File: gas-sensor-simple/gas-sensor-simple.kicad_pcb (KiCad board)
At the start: 2 copper layers, 29 parts, among them J1 8-pin male, U1 MQ-8, U10 MV5x3x, U11 MV5x3x, U12 LM393, U13 ads1x15, U14 ads1x15, U15 BME280, U2 MQ-4, U3 CO2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

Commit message: Minor change to pcb
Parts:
- moved R8 3.81 mm to (171.4, 138.4)
- moved R2 2.54 mm to (171.4, 96.5)
- moved R4 2.54 mm to (171.4, 110.5)
- moved R6 2.54 mm to (171.4, 124.5)
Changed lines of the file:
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@@
     (links 89)
     (no_connects 89)
-    (area 94.431429 79.964999 179.491905 150.725)
+    (area 102.051429 78.694999 183.301905 150.725)
     (thickness 1.6)
     (drawings 0)
@@
     (pad_to_mask_clearance 0.2)
     (aux_axis_origin 0 0)
-    (visible_elements FFFFF77F)
+    (visible_elements 7FFFFFFF)
     (pcbplotparams
       (layerselection 0x00030_80000001)
@@
   )
   (module Resistors_THT:R_Axial_DIN0207_L6.3mm_D2.5mm_P10.16mm_Horizontal (layer F.Cu)
-    (at 171.45 93.98 90)
+    (at 171.45 96.52 90)
     (descr "Resistor, Axial_DIN0207 series, Axial, Horizontal, pin pitch=10.16mm, 0.25W = 1/4W, length*diameter=6.3*2.5mm^2, http://cdn-reichelt.de/documents/datenblatt/B400/1_4W%23YAG.pdf")
     (tags "Resistor Axial_DIN0207 series Axial Horizontal pin pitch 10.16mm 0.25W = 1/4W length 6.3mm diameter 2.5mm")
@@
   )
   (module Resistors_THT:R_Axial_DIN0207_L6.3mm_D2.5mm_P10.16mm_Horizontal (layer F.Cu)
-    (at 171.45 107.95 90)
+    (at 171.45 110.49 90)
     (descr "Resistor, Axial_DIN0207 series, Axial, Horizontal, pin pitch=10.16mm, 0.25W = 1/4W, length*diameter=6.3*2.5mm^2, http://cdn-reichelt.de/documents/datenblatt/B400/1_4W%23YAG.pdf")
     (tags "Resistor Axial_DIN0207 series Axial Horizontal pin pitch 10.16mm 0.25W = 1/4W length 6.3mm diameter 2.5mm")
@@
   )
   (module Resistors_THT:R_Axial_DIN0207_L6.3mm_D2.5mm_P10.16mm_Horizontal (layer F.Cu)
-    (at 171.45 121.92 90)
+    (at 171.45 124.46 90)
     (descr "Resistor, Axial_DIN0207 series, Axial, Horizontal, pin pitch=10.16mm, 0.25W = 1/4W, length*diameter=6.3*2.5mm^2, http://cdn-reichelt.de/documents/datenblatt/B400/1_4W%23YAG.pdf")
     (tags "Resistor Axial_DIN0207 series Axial Horizontal pin pitch 10.16mm 0.25W = 1/4W length 6.3mm diameter 2.5mm")
@@
   )
   (module Resistors_THT:R_Axial_DIN0207_L6.3mm_D2.5mm_P10.16mm_Horizontal (layer F.Cu)
-    (at 171.45 134.62 90)
-    (descr "Resistor, Axial_DIN0207 series, Axial, Horizontal, pin pitch=10.16mm, 0.25W = 1/4W, length*diameter=6.3*2.5mm^2, http://cdn-reichelt.de/documents/datenblatt/B400/1_4W%23YAG.pdf")
-    (tags "Resistor Axial_DIN0207 series Axial Horizontal pin pitch 10.16mm 0.25W = 1/4W length 6.3mm diameter 2.5mm")
+    (at 171.45 138.43 90)
+    (descr "Resistor, Axial_DIN0207 series, Axial, Horizontal, pin pitch=10.16mm, 0.25W = 1/4W, length*diameter=6.3*2.5mm^2, http://cdn-reichelt.de/documents/datenblatt/B400/1_4W%23YAG.pdf")
+    (tags "Resistor Axial_DIN0207 series Axial Horizontal pin pitch 10.16mm 0.25W = 1/4W length 6.3mm diameter 2.5mm")

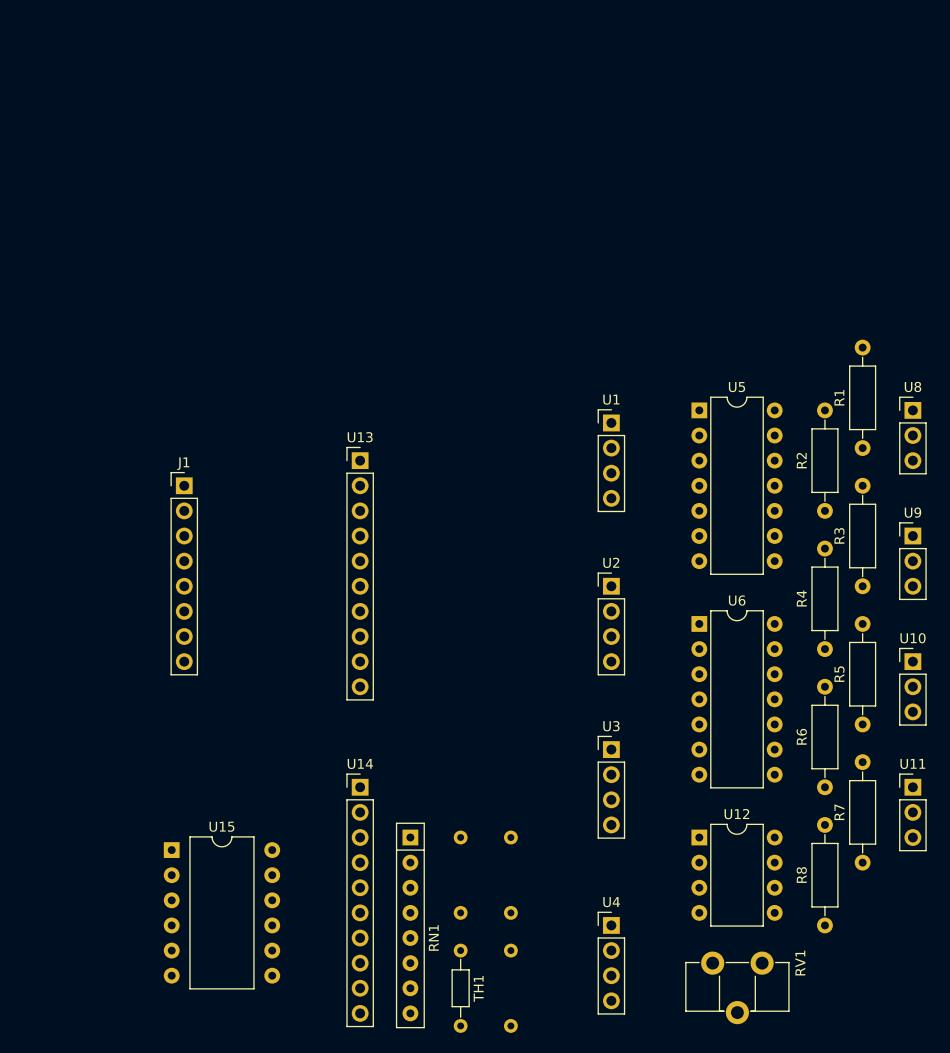
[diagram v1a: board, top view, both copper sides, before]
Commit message: Add back headers to separate analog board from digital.
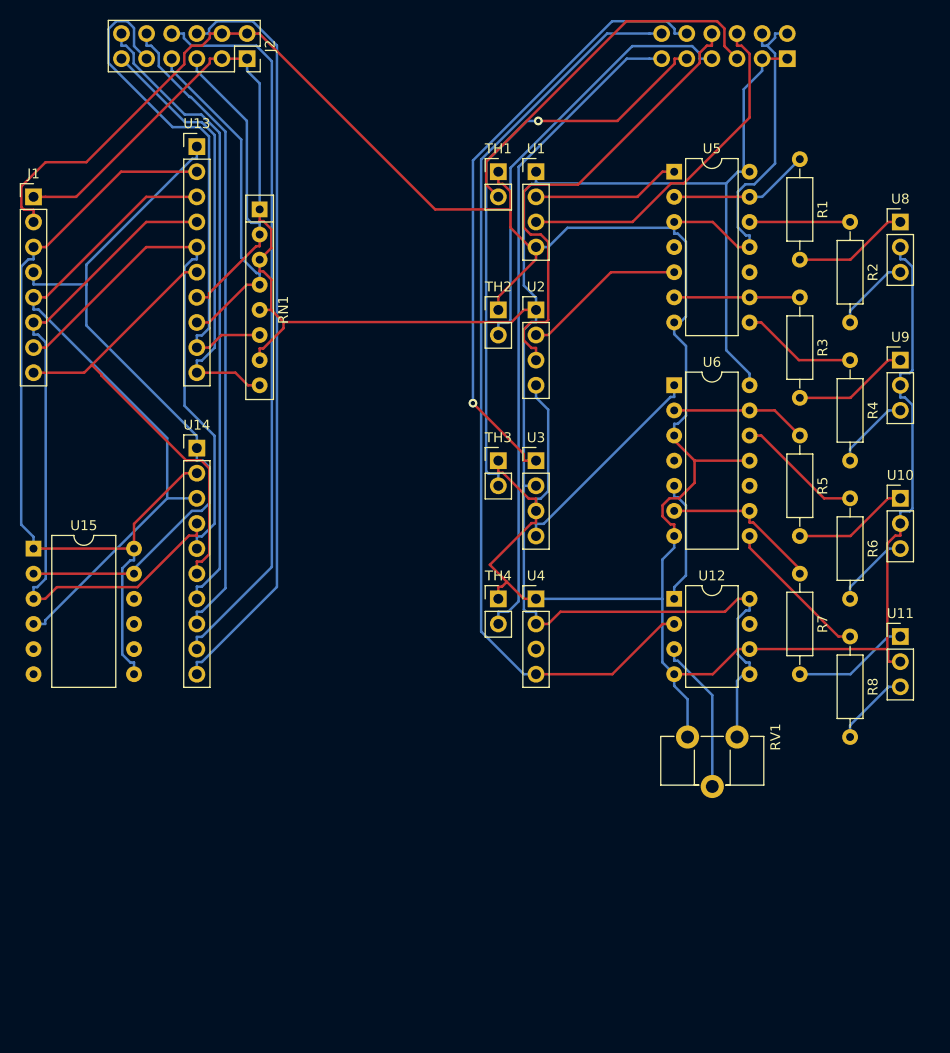
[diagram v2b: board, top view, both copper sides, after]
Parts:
- added J2: 2 x 6 pin female, Socket_Strips:Socket_Strip_Straight_2x06_Pitch2.54mm, F.Cu at (113.0, 50.8)
- added J3: 2 x 6 pin male, Pin_Headers:Pin_Header_Straight_2x06_Pitch2.54mm, B.Cu at (167.6, 50.8)
- J1: value 8-pin male -> 8-pin
- TH1: footprint Resistors_THT:R_Axial_DIN0204_L3.6mm_D1.6mm_P7.62mm_Horizontal -> Socket_Strips:Socket_Strip_Straight_1x02_Pitch2.54mm
- TH2, TH3, TH4: footprint Resistors_THT:R_Axial_DIN0204_L3.6mm_D1.6mm_P7.62mm_Horizontal -> Socket_Strips:Socket_Strip_Straight_1x02_Pitch2.54mm; moved to F.Cu
- U3: value CO2 -> DFRobotCO2; footprint Pin_Headers:Pin_Header_Straight_1x04_Pitch2.54mm -> Socket_Strips:Socket_Strip_Straight_1x04_Pitch2.54mm
- moved TH1 78.8 mm to (138.4, 62.2), turned to 0 degrees
- moved RN1 65.3 mm to (114.3, 66.0)
- moved TH2 53.4 mm to (138.4, 76.2), turned to 0 degrees
- moved TH3 38.3 mm to (138.4, 91.4), turned to 0 degrees
- moved U14 38.1 mm to (108.0, 90.2)
- moved U13 35.8 mm to (108.0, 59.7)
- moved TH4 35.6 mm to (138.4, 105.4), turned to 0 degrees
- moved U4 33.9 mm to (142.2, 105.4)
- moved U15 33.5 mm to (91.4, 100.3)
- moved J1 32.9 mm to (91.4, 64.8)
- moved U3 30.2 mm to (142.2, 91.4)
- moved R7 29.9 mm to (168.9, 102.9), turned to 270 degrees
- moved R1 29.9 mm to (168.9, 61.0), turned to 270 degrees
- moved R3 29.9 mm to (168.9, 74.9), turned to 270 degrees
- moved R5 29.9 mm to (168.9, 88.9), turned to 270 degrees
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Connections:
- J1 pad 1: Net-(J1-Pad1) -> VCC
- J1 pad 2: +3V3 -> GND
- J1 pad 3: GND -> GNDD
- J1 pad 4: VCC -> +3V3
- RN1 pad 1: Net-(RN1-Pad1) -> VCC
- RN1 pad 2: VCC -> Net-(J2-Pad5)
- RN1 pad 3: Net-(RN1-Pad3) -> VCC
- RN1 pad 4: VCC -> Net-(J2-Pad7)
- RN1 pad 5: Net-(RN1-Pad5) -> VCC
- RN1 pad 6: VCC -> Net-(J2-Pad9)
- RN1 pad 7: Net-(RN1-Pad7) -> VCC
- RN1 pad 8: VCC -> Net-(J2-Pad11)
- TH1 pad 1: Net-(RN1-Pad1) -> GND
- TH1 pad 2: GND -> Net-(J3-Pad5)
- TH2 pad 1: Net-(RN1-Pad3) -> GND
- TH2 pad 2: GND -> Net-(J3-Pad7)
- TH3 pad 1: Net-(RN1-Pad5) -> GND
- TH3 pad 2: GND -> Net-(J3-Pad9)
- TH4 pad 1: Net-(RN1-Pad7) -> GND
- TH4 pad 2: GND -> Net-(J3-Pad11)
- U1 pad 3: Net-(U1-Pad3) -> Net-(J3-Pad6)
- U12 pad 2: Net-(U12-Pad2) -> Net-(J3-Pad12)
- U13 pad 1: VCC -> +3V3
- U13 pad 10: Net-(U12-Pad2) -> Net-(J2-Pad11)
- U13 pad 2: GND -> GNDD
- U13 pad 7: Net-(U1-Pad3) -> Net-(J2-Pad5)
- U13 pad 8: Net-(U13-Pad8) -> Net-(J2-Pad7)
- U13 pad 9: Net-(U13-Pad9) -> Net-(J2-Pad9)
- U14 pad 1: VCC -> +3V3
- U14 pad 10: Net-(RN1-Pad7) -> Net-(J2-Pad6)
- U14 pad 2: GND -> GNDD
- U14 pad 5: Net-(U14-Pad5) -> Net-(J1-Pad7)
- U14 pad 6: Net-(U14-Pad6) -> Net-(J1-Pad8)
- U14 pad 7: Net-(RN1-Pad1) -> Net-(J2-Pad12)
- U14 pad 8: Net-(RN1-Pad3) -> Net-(J2-Pad10)
- U14 pad 9: Net-(RN1-Pad5) -> Net-(J2-Pad8)
- U15 pad 1: GND -> GNDD
- U15 pad 10: GND -> Net-(U15-Pad10)
- U15 pad 11: (no net) -> +3V3
- U15 pad 12: (no net) -> GNDD
- U15 pad 5: GND -> Net-(U15-Pad5)
- U15 pad 7: Net-(U15-Pad7) -> GNDD
- U15 pad 9: +3V3 -> Net-(U15-Pad9)
- U2 pad 3: Net-(U13-Pad8) -> Net-(J3-Pad8)
- U3 pad 1: Net-(U13-Pad9) -> Net-(J3-Pad10)
- U4 pad 4: Net-(U12-Pad2) -> Net-(J3-Pad12)
- U5 pad 12: Net-(U5-Pad12) -> Net-(R2-Pad1)
- U5 pad 13: GND -> Net-(R1-Pad1)
- U5 pad 3: Net-(R1-Pad1) -> GND
- U5 pad 4: Net-(R2-Pad1) -> Net-(U5-Pad4)
- U6 pad 12: Net-(U6-Pad12) -> Net-(R6-Pad1)
- U6 pad 13: GND -> Net-(R5-Pad1)
- U6 pad 3: Net-(U3-Pad4) -> GND
- U6 pad 4: Net-(R6-Pad1) -> Net-(U6-Pad4)
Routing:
- net GND: track 0.00 -> 324.5 mm
- net VCC: track 0.00 -> 237.0 mm
- net Net-(J3-Pad12): track 0.00 -> 94.7 mm
- net GNDD: track 0.00 -> 86.7 mm
- net Net-(J2-Pad6): track 0.00 -> 77.1 mm
- net Net-(J2-Pad8): track 0.00 -> 74.4 mm
- net +3V3: track 0.00 -> 74.0 mm
- net Net-(J1-Pad6): track 0.00 -> 70.6 mm
- net Net-(J1-Pad5): track 0.00 -> 68.9 mm
- net Net-(J3-Pad11): track 0.00 -> 66.6 mm
- net Net-(J2-Pad10): track 0.00 -> 64.8 mm
- net Net-(J2-Pad12): track 0.00 -> 63.8 mm
- net Net-(J3-Pad10): track 0.00 -> 61.9 mm, vias 0 -> 1
- net Net-(J3-Pad9): track 0.00 -> 58.8 mm, vias 0 -> 1
- net Net-(J1-Pad7): track 0.00 -> 54.3 mm
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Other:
- net class Default: clearance 0.2 -> 0.254; trace_width 0.25 -> 0.254; via_dia 0.6 -> 0.889; via_drill 0.4 -> 0.635
- rule pad_to_mask_clearance: 0.2 -> 0
- rule trace_clearance: 0.2 -> 0.254
- rule trace_min: 0.2 -> 0.254
- rule via_min_drill: 0.3 -> 0.635
- rule via_min_size: 0.4 -> 0.889

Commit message: Start adding capacitors and improve PCB layout.
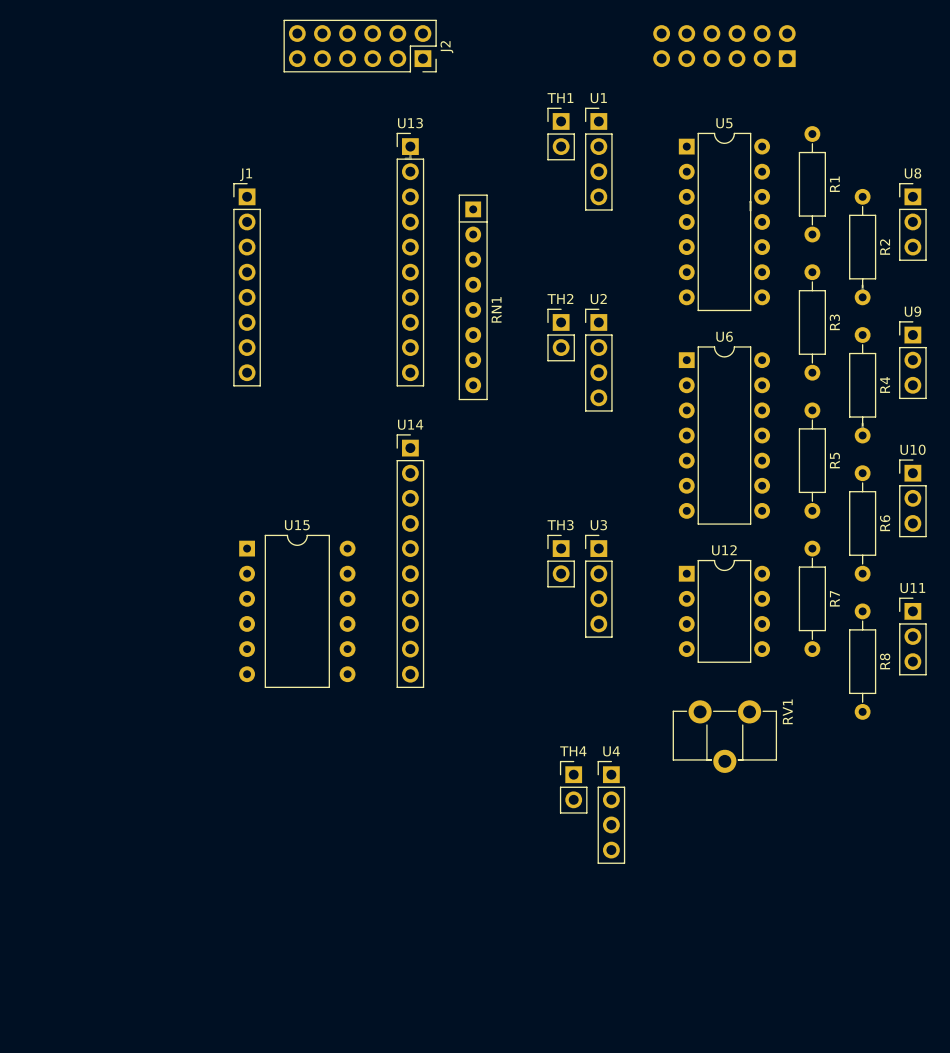
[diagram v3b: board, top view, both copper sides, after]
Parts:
- moved J1 21.6 mm to (113.0, 64.8)
- moved U15 21.6 mm to (113.0, 100.3)
- moved RN1 21.6 mm to (135.9, 66.0)
- moved U13 21.6 mm to (129.5, 59.7)
- moved U14 21.6 mm to (129.5, 90.2)
- moved TH4 19.3 mm to (146.1, 123.2)
- moved U4 19.3 mm to (149.9, 123.2)
- moved J2 17.8 mm to (130.8, 50.8)
- moved TH3 10.9 mm to (144.8, 100.3)
- moved U3 10.9 mm to (148.6, 100.3)
- moved TH1 8.13 mm to (144.8, 57.1)
- moved U1 8.13 mm to (148.6, 57.1)
- moved TH2 6.48 mm to (144.8, 77.5)
- moved U2 6.48 mm to (148.6, 77.5)
- moved R3 2.84 mm to (170.2, 72.4)
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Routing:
- net GND: track 324.5 -> 0.00 mm
- net VCC: track 237.0 -> 0.00 mm
- net Net-(J3-Pad12): track 94.7 -> 0.00 mm
- net GNDD: track 86.7 -> 0.00 mm
- net Net-(J2-Pad6): track 77.1 -> 0.00 mm
- net Net-(J2-Pad8): track 74.4 -> 0.00 mm
- net +3V3: track 74.0 -> 2.19 mm
- net Net-(J1-Pad6): track 70.6 -> 0.00 mm
- net Net-(J1-Pad5): track 68.9 -> 0.00 mm
- net Net-(J3-Pad11): track 66.6 -> 0.00 mm
- net Net-(J2-Pad10): track 64.8 -> 0.00 mm
- net Net-(J2-Pad12): track 63.8 -> 0.00 mm
- net Net-(J3-Pad10): track 61.9 -> 0.00 mm, vias 1 -> 0
- net Net-(J3-Pad9): track 58.8 -> 0.00 mm, vias 1 -> 0
- net Net-(J1-Pad7): track 54.3 -> 0.01 mm
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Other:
- net class Default: trace_width 0.254 -> 0.381
- rule trace_min: 0.254 -> 0.381
